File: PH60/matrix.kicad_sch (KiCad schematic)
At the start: 124 parts

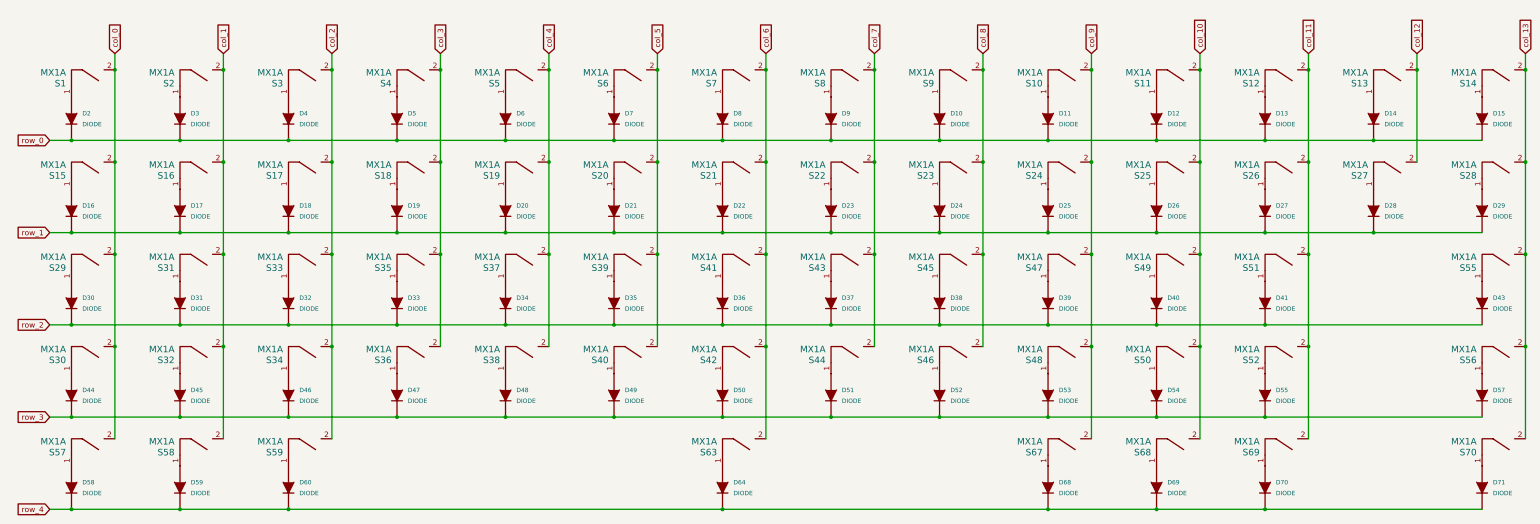
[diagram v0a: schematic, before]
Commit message: Remodel whole system to nrfmicro
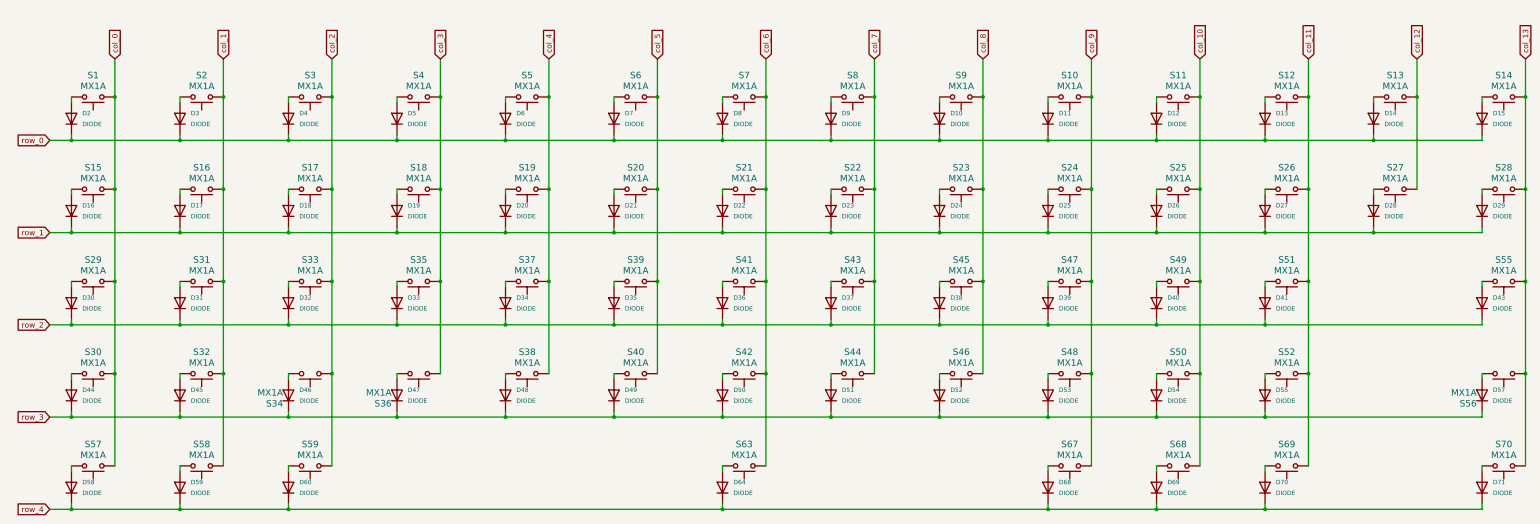
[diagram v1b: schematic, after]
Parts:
- D10, D11, D12, D13, D14, D15, D16, D17, D18, D19, D2, D20, D21, D22, D23, D24, D25, D26, D27, D28, D29, D3, D30, D31, D32, D33, D34, D35, D36, D37, D38, D39, D4, D40, D41, D43, D44, D45, D46, D47, D48, D49, D5, D50, D51, D52, D53, D54, D55, D57, D58, D59, D6, D60, D64, D68, D69, D7, D70, D71, D8, D9: footprint 0805:0805D -> Diode_SMD:D_0805_2012Metric_Pad1.15x1.40mm_HandSolder; symbol device:DIODE -> Device:D
- S1, S10, S11, S12, S13, S16, S17, S18, S19, S2, S20, S21, S22, S23, S24, S25, S26, S27, S3, S31, S32, S33, S34, S35, S36, S37, S38, S39, S4, S40, S41, S42, S43, S44, S45, S46, S47, S48, S49, S5, S50, S51, S52, S55, S6, S7, S8, S9: footprint Button_Switch_Keyboard:SW_Cherry_MX_1.00u_PCB -> PCM_Switch_Keyboard_Hotswap_Kailh:SW_Hotswap_Kailh_MX_1.00u; symbol mx1a-simple:MX1A -> Switch:SW_Push
- S14: footprint Button_Switch_Keyboard:SW_Cherry_MX_2.00u_PCB -> PCM_Switch_Keyboard_Hotswap_Kailh:SW_Hotswap_Kailh_MX_2.00u; symbol mx1a-simple:MX1A -> Switch:SW_Push
- S15: footprint Button_Switch_Keyboard:SW_Cherry_MX_1.50u_PCB -> PCM_Switch_Keyboard_Hotswap_Kailh:SW_Hotswap_Kailh_MX_1.50u; symbol mx1a-simple:MX1A -> Switch:SW_Push
- S28: footprint Button_Switch_Keyboard:SW_Cherry_MX_ISOEnter_PCB -> PCM_Switch_Keyboard_Hotswap_Kailh:SW_Hotswap_Kailh_MX_ISOEnter; symbol mx1a-simple:MX1A -> Switch:SW_Push
- S29: footprint Button_Switch_Keyboard:SW_Cherry_MX_1.75u_PCB -> PCM_Switch_Keyboard_Hotswap_Kailh:SW_Hotswap_Kailh_MX_1.75u; symbol mx1a-simple:MX1A -> Switch:SW_Push
- S30, S57, S58, S59, S67, S68, S69, S70: footprint Button_Switch_Keyboard:SW_Cherry_MX_1.25u_PCB -> PCM_Switch_Keyboard_Hotswap_Kailh:SW_Hotswap_Kailh_MX_1.25u; symbol mx1a-simple:MX1A -> Switch:SW_Push
- S56: footprint Button_Switch_Keyboard:SW_Cherry_MX_2.75u_PCB -> PCM_Switch_Keyboard_Hotswap_Kailh:SW_Hotswap_Kailh_MX_2.75u; symbol mx1a-simple:MX1A -> Switch:SW_Push
- S63: footprint Button_Switch_Keyboard:SW_Cherry_MX_6.25u_PCB -> PCM_Switch_Keyboard_Hotswap_Kailh:SW_Hotswap_Kailh_MX_6.25u; symbol mx1a-simple:MX1A -> Switch:SW_Push
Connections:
- net row_0: now also D10.1 (K), D11.1 (K), D12.1 (K), D13.1 (K), D14.1 (K), D15.1 (K), D2.1 (K), D3.1 (K), D4.1 (K), D5.1 (K), D6.1 (K), D7.1 (K), D8.1 (K), D9.1 (K); no longer D10.2 (K), D11.2 (K), D12.2 (K), D13.2 (K), D14.2 (K), D15.2 (K), D2.2 (K), D3.2 (K), D4.2 (K), D5.2 (K), D6.2 (K), D7.2 (K), D8.2 (K), D9.2 (K)
- net row_1: now also D16.1 (K), D17.1 (K), D18.1 (K), D19.1 (K), D20.1 (K), D21.1 (K), D22.1 (K), D23.1 (K), D24.1 (K), D25.1 (K), D26.1 (K), D27.1 (K), D28.1 (K), D29.1 (K); no longer D16.2 (K), D17.2 (K), D18.2 (K), D19.2 (K), D20.2 (K), D21.2 (K), D22.2 (K), D23.2 (K), D24.2 (K), D25.2 (K), D26.2 (K), D27.2 (K), D28.2 (K), D29.2 (K)
- net row_2: now also D30.1 (K), D31.1 (K), D32.1 (K), D33.1 (K), D34.1 (K), D35.1 (K), D36.1 (K), D37.1 (K), D38.1 (K), D39.1 (K), D40.1 (K), D41.1 (K), D43.1 (K); no longer D30.2 (K), D31.2 (K), D32.2 (K), D33.2 (K), D34.2 (K), D35.2 (K), D36.2 (K), D37.2 (K), D38.2 (K), D39.2 (K), D40.2 (K), D41.2 (K), D43.2 (K)
- net row_3: now also D44.1 (K), D45.1 (K), D46.1 (K), D47.1 (K), D48.1 (K), D49.1 (K), D50.1 (K), D51.1 (K), D52.1 (K), D53.1 (K), D54.1 (K), D55.1 (K), D57.1 (K); no longer D44.2 (K), D45.2 (K), D46.2 (K), D47.2 (K), D48.2 (K), D49.2 (K), D50.2 (K), D51.2 (K), D52.2 (K), D53.2 (K), D54.2 (K), D55.2 (K), D57.2 (K)
- net row_4: now also D58.1 (K), D59.1 (K), D60.1 (K), D64.1 (K), D68.1 (K), D69.1 (K), D70.1 (K), D71.1 (K); no longer D58.2 (K), D59.2 (K), D60.2 (K), D64.2 (K), D68.2 (K), D69.2 (K), D70.2 (K), D71.2 (K)
- net at S37.1: now also D34.2 (A); no longer D34.1 (A)
- net at S9.1: now also D10.2 (A); no longer D10.1 (A)
- net at S70.1: now also D71.2 (A); no longer D71.1 (A)
- net at S14.1: now also D15.2 (A); no longer D15.1 (A)
- net at S38.1: now also D48.2 (A); no longer D48.1 (A)
- net at S58.1: now also D59.2 (A); no longer D59.1 (A)
- net at S2.1: now also D3.2 (A); no longer D3.1 (A)
- net at S32.1: now also D45.2 (A); no longer D45.1 (A)
- net at S7.1: now also D8.2 (A); no longer D8.1 (A)
- net at S30.1: now also D44.2 (A); no longer D44.1 (A)
- net at S16.1: now also D17.2 (A); no longer D17.1 (A)
- net at S68.1: now also D69.2 (A); no longer D69.1 (A)
- net at S63.1: now also D64.2 (A); no longer D64.1 (A)
- net at S51.1: now also D41.2 (A); no longer D41.1 (A)
- net at S48.1: now also D53.2 (A); no longer D53.1 (A)
- net at S41.1: now also D36.2 (A); no longer D36.1 (A)
- net at S34.1: now also D46.2 (A); no longer D46.1 (A)
- net at S28.1: now also D29.2 (A); no longer D29.1 (A)
- net at S40.1: now also D49.2 (A); no longer D49.1 (A)
- net at S13.1: now also D14.2 (A); no longer D14.1 (A)
- net at S23.1: now also D24.2 (A); no longer D24.1 (A)
- net at S18.1: now also D19.2 (A); no longer D19.1 (A)
- net at S3.1: now also D4.2 (A); no longer D4.1 (A)
- net at S24.1: now also D25.2 (A); no longer D25.1 (A)
- net at S36.1: now also D47.2 (A); no longer D47.1 (A)
- net at S1.1: now also D2.2 (A); no longer D2.1 (A)
- net at S31.1: now also D31.2 (A); no longer D31.1 (A)
- net at S11.1: now also D12.2 (A); no longer D12.1 (A)
- net at S55.1: now also D43.2 (A); no longer D43.1 (A)
- net at S4.1: now also D5.2 (A); no longer D5.1 (A)
- net at S59.1: now also D60.2 (A); no longer D60.1 (A)
- net at S35.1: now also D33.2 (A); no longer D33.1 (A)
- net at S69.1: now also D70.2 (A); no longer D70.1 (A)
- net at S25.1: now also D26.2 (A); no longer D26.1 (A)
- net at S15.1: now also D16.2 (A); no longer D16.1 (A)
- net at S49.1: now also D40.2 (A); no longer D40.1 (A)
- net at S8.1: now also D9.2 (A); no longer D9.1 (A)
- net at S44.1: now also D51.2 (A); no longer D51.1 (A)
- net at S50.1: now also D54.2 (A); no longer D54.1 (A)
- net at S19.1: now also D20.2 (A); no longer D20.1 (A)
- net at S46.1: now also D52.2 (A); no longer D52.1 (A)
- net at S67.1: now also D68.2 (A); no longer D68.1 (A)
- net at S21.1: now also D22.2 (A); no longer D22.1 (A)
- net at S22.1: now also D23.2 (A); no longer D23.1 (A)
- net at S45.1: now also D38.2 (A); no longer D38.1 (A)
- net at S42.1: now also D50.2 (A); no longer D50.1 (A)
- net at S52.1: now also D55.2 (A); no longer D55.1 (A)
- net at S27.1: now also D28.2 (A); no longer D28.1 (A)
- net at S57.1: now also D58.2 (A); no longer D58.1 (A)
- net at S10.1: now also D11.2 (A); no longer D11.1 (A)
- net at S33.1: now also D32.2 (A); no longer D32.1 (A)
- net at S39.1: now also D35.2 (A); no longer D35.1 (A)
- net at S12.1: now also D13.2 (A); no longer D13.1 (A)
- net at S29.1: now also D30.2 (A); no longer D30.1 (A)
- net at S6.1: now also D7.2 (A); no longer D7.1 (A)
- net at S43.1: now also D37.2 (A); no longer D37.1 (A)
- net at S5.1: now also D6.2 (A); no longer D6.1 (A)
- net at S20.1: now also D21.2 (A); no longer D21.1 (A)
- net at S26.1: now also D27.2 (A); no longer D27.1 (A)
- net at S17.1: now also D18.2 (A); no longer D18.1 (A)
- net at S56.1: now also D57.2 (A); no longer D57.1 (A)
- net at S47.1: now also D39.2 (A); no longer D39.1 (A)
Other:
- moved on the sheet: D10, D11, D12, D13, D14, D15, D16, D17, D18, D19, D2, D20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

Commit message: PCB Updates
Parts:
- renumbered D2 to D1, D11 to D10, D12 to D11, D13 to D12, D14 to D13, D15 to D14, D16 to D15, D17 to D16, D18 to D17, D19 to D18, D20 to D19, D3 to D2, D21 to D20, D22 to D21, D23 to D22, D24 to D23, D25 to D24, D26 to D25, D27 to D26, D28 to D27, D29 to D28, D30 to D29, D4 to D3, D31 to D30, D32 to D31, D33 to D32, D34 to D33, D35 to D34, D36 to D35, D37 to D36, D38 to D37, D39 to D38, D40 to D39, D5 to D4, D41 to D40, D43 to D41, D44 to D42, D45 to D43, D46 to D44, D47 to D45, D48 to D46, D49 to D47, D50 to D48, D51 to D49, D6 to D5, D52 to D50, D53 to D51, D54 to D52, D55 to D53, D57 to D54, D58 to D55, D59 to D56, D60 to D57, D64 to D58, D68 to D59, D7 to D6, D69 to D60, D70 to D61, D71 to D62, D8 to D7, D9 to D8, D10 to D9, S31 to S30, S33 to S31, S35 to S32, S37 to S33, S39 to S34, S41 to S35, S43 to S36, S45 to S37, S47 to S38, S49 to S39, S51 to S40, S55 to S41, S30 to S42, S32 to S43, S34 to S44, S36 to S45, S38 to S46, S40 to S47, S42 to S48, S44 to S49, S46 to S50, S48 to S51, S50 to S52, S52 to S53, S56 to S54, S57 to S55, S58 to S56, S59 to S57, S63 to S58, S67 to S59, S68 to S60, S69 to S61, S70 to S62
